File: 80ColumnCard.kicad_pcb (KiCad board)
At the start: 2 copper layers, 155.2 x 78.6 mm, 47 parts, among them J1 Apple II Expansion Bus, J2 VIDEO & LIGHT PEN, Q1 2N3904, U1 74LS86, U10N24 6116, U10N28 '32 - '256, U10N32 '512, U10W24 6116, U10W28 '32 - '256, U10W32 '512, U14 74LS157, U15 74LS157, U16 74LS157, U18 74LS273, U19 MC6845, U2 74LS02, U20 2732, U20B1 '64 - '512, U20C1 '010 - '080, U21 74LS166, U22 74LS175, U23 74LS161, U3 2758/16/32, U4 74LS04, U5 74LS245, U6 74LS00, U7 4013, U8 4013, U9 74LS139, X6 CHAR INV, X7 SCREEN INV, X99 WE/A11, Y1 17.430 MHZ

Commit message: updates
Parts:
- added U3W28: '64 - '512, Package_DIP:DIP-28_W15.24mm, F.Cu at (168.9, 87.6)
- U3: value 2758/16/32 -> 2758/'16/'32
- X21: renamed from X99; value WE/A11 -> A11/WE; footprint Jumper:SolderJumper-3_P1.3mm_Bridged12_RoundedPad1.0x1.5mm_NumberLabels -> MyPassives:SolderJumper-3_Pie_Bridged12; moved to F.Cu
- moved X21 12.1 mm to (114.9, 111.1)
- moved U9 2.54 mm to (168.9, 83.8)
- moved CR1 1.27 mm to (190.5, 80.0)
- renumbered U10N24 to U10
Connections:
- net /RAMAB renamed /RAM_~{A}/B
- net Net-(U2-Pad13) renamed /Firmware/~{OE}
- net Net-(U3-Pad22) renamed /Firmware/A9
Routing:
- net +5V: track 807.0 -> 834.8 mm
- net /SRAM/RAMA11: track 60.0 -> 75.0 mm, vias 1 -> 2
- net /SRAM/RAM_R/~{W}: track 91.8 -> 104.4 mm, vias 0 -> 1
- net GND: track 806.0 -> 816.5 mm
- net Net-(U10-Pad21): track 3.81 -> 11.8 mm, vias 0 -> 1
- net /Firmware/A9: track 32.5 -> 38.5 mm
- net Net-(U19-Pad19): track 94.7 -> 100.6 mm
- net /R/~{W}: track 128.2 -> 133.3 mm
- net /~{DEV}: track 37.7 -> 42.6 mm
- net /D2: track 87.3 -> 92.1 mm
- net /D1: track 76.0 -> 80.1 mm
- net /~{RES}: track 132.7 -> 136.8 mm
- net Net-(U19-Pad18): track 76.1 -> 79.9 mm
- net /D0: track 84.0 -> 87.8 mm
- net /ROMA0: track 48.0 -> 51.7 mm
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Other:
- board text removed: "1-2 6116 2-3 6132-61512"

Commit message: tweak
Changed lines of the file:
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@@
       (disableapertmacros false)
       (usegerberextensions false)
-      (usegerberattributes true)
+      (usegerberattributes false)
       (usegerberadvancedattributes true)
       (creategerberjobfile true)
@@
   (arc (start 215.528025 80.01) (mid 214.698358 79.844969) (end 213.995 79.375) (width 0.25) (layer "F.Cu") (net 21))
   (arc (start 223.52 77.47) (mid 222.776051 79.266051) (end 220.98 80.01) (width 0.25) (layer "F.Cu") (net 21))
+  (segment (start 175.26 83.928949) (end 175.26 83.82) (width 0.25) (layer "F.Cu") (net 22))
   (segment (start 190.5 113.03) (end 186.055 106.68) (width 0.25) (layer "F.Cu") (net 22))
   (segment (start 194.31 117.475) (end 190.5 113.03) (width 0.25) (layer "F.Cu") (net 22))
-  (segment (start 175.26 83.82) (end 175.26 85.725) (width 0.25) (layer "F.Cu") (net 22))
   (segment (start 180.34 96.193153) (end 180.34 98.425) (width 0.25) (layer "F.Cu") (net 22))
   (segment (start 185.869013 106.494013) (end 186.055 106.68) (width 0.25) (layer "F.Cu") (net 22))
@@
   (arc (start 173.355 81.915) (mid 174.702038 82.472962) (end 175.26 83.82) (width 0.25) (layer "F.Cu") (net 22))
   (arc (start 199.39 127) (mid 198.573138 122.893356) (end 196.24691 119.411911) (width 0.25) (layer "F.Cu") (net 22))
-  (arc (start 175.26 85.725) (mid 175.631974 86.623026) (end 176.53 86.995) (width 0.25) (layer "F.Cu") (net 22))
+  (arc (start 176.53 86.995) (mid 175.590062 85.588284) (end 175.26 83.928949) (width 0.25) (layer "F.Cu") (net 22))
   (arc (start 185.42 105.41) (mid 185.536695 105.996664) (end 185.869013 106.494013) (width 0.25) (layer "F.Cu") (net 22))
   (arc (start 183.065987 103.690987) (mid 183.563336 104.023305) (end 184.15 104.14) (width 0.25) (layer "F.Cu") (net 22))

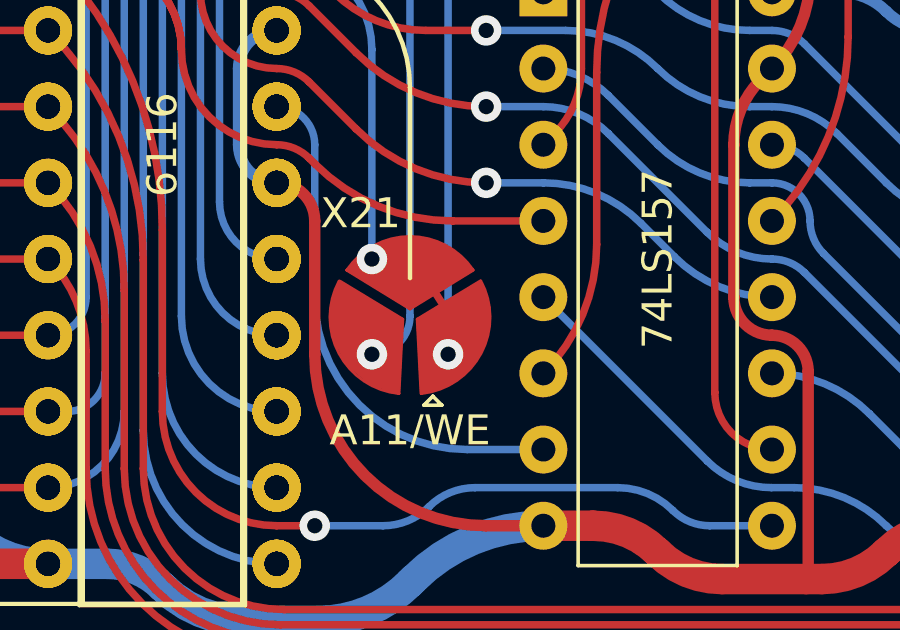
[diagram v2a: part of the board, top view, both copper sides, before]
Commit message: rename alternate char rom footprints
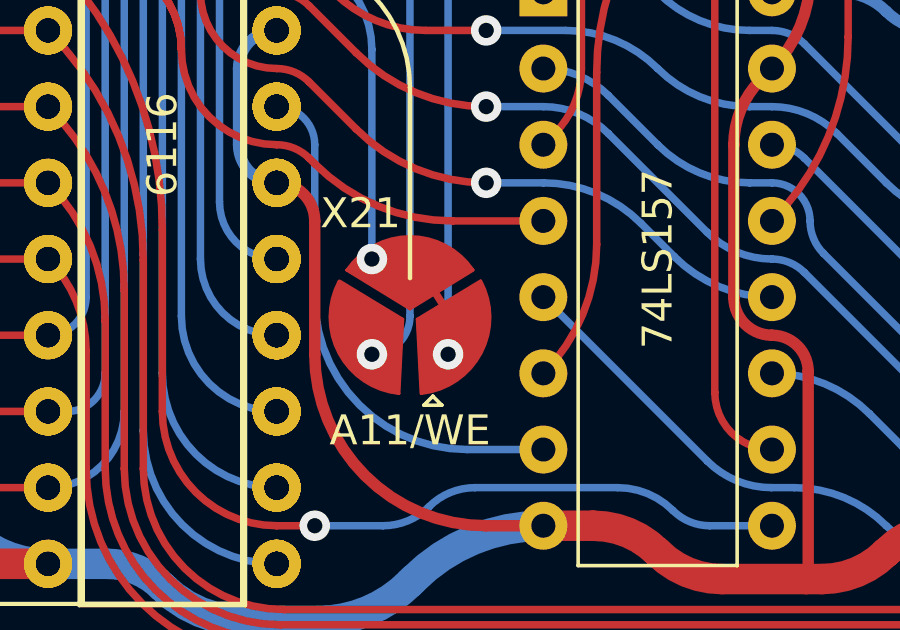
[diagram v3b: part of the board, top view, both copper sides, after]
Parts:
- renumbered U20B1 to U20W28, U20C1 to U20W32
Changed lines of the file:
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@@
     (property "Sheetname" "Character ROM")
     (attr through_hole)
-    (fp_text reference "U20C1" (at 7.62 -2.33 90) (layer "F.SilkS") hide
+    (fp_text reference "U20W32" (at 7.62 -2.33 90) (layer "F.SilkS") hide
       (effects (font (size 1 1) (thickness 0.15)))
     )
@@
       (primitives
         (gr_line (start 0.254 -0.5715) (end -2.2225 -0.4445) (width 0.1))
-    (gr_arc (start 1.535357 1.544921) (mid -0.867077 1.562872) (end -2.220191 -0.422348) (width 0.1))
+    (gr_arc (start 1.535357 1.544921) (mid -0.865104 1.563904) (end -2.219705 -0.41792) (width 0.1))
         (gr_line (start 0.254 -0.5715) (end 1.524 1.524) (width 0.1))
         (gr_poly (pts
@@
             (gr_line (start 0.720183 -2.106487) (end -0.5715 0) (width 0.1))
     (gr_arc (start 0.720183 -2.106487) (mid 1.541357 -1.196944) (end 1.84148 -0.00887) (width 0.1))
-    (gr_arc (start 1.8415 0) (mid 1.547018 1.186649) (end 0.732292 2.098283) (width 0.1))
+    (gr_arc (start 1.8415 0) (mid 1.548053 1.184689) (end 0.735952 2.095783) (width 0.1))
       ))
     (pad "3" smd custom (at -0.3556 -0.8128 90) (size 0.0254 0.0254) (layers "F.Cu" "F.Mask")
@@
     (property "Sheetname" "Character ROM")
     (attr through_hole)
-    (fp_text reference "U20B1" (at 7.62 -2.33 90) (layer "F.SilkS") hide
-      (effects (font (size 1 1) (thickness 0.15)))
-    )
+    (fp_text reference "U20W28" (at 7.62 -2.33 90) (layer "F.SilkS") hide
+      (effects (font (size 1 1) (thickness 0.15)))
+    )
